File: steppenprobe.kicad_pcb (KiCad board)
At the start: 2 copper layers, 50 x 60 mm, 75 parts, among them J1 USB_C_Receptacle_USB2.0, J2 Conn_01x12, U1 SRV05-4, U2 XC6206PxxxMR, U3 FT2232HL, U4 74LVC1G125, U5 74LVC1G125, U6 74LVC1G125, U7 74LVC1G125, U8 74LVC1G125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

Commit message: Reworked oscillator placement. Fixed silkscreen, added arrows.
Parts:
- moved C5 3.09 mm to (132.0, 67.2), turned to -90 degrees
- moved Y1 2.83 mm to (134.8, 67.0)
- moved C3 1.25 mm to (137.5, 67.2), turned to 90 degrees
- moved FB3 1.13 mm to (132.8, 63.7), turned to 0 degrees
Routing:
- net GND: track 97.0 -> 85.1 mm, vias 39 -> 38
- net /OSCO: track 11.1 -> 8.11 mm
- net /OSCI: track 12.3 -> 13.6 mm
- net /VPHY: track 7.34 -> 8.02 mm

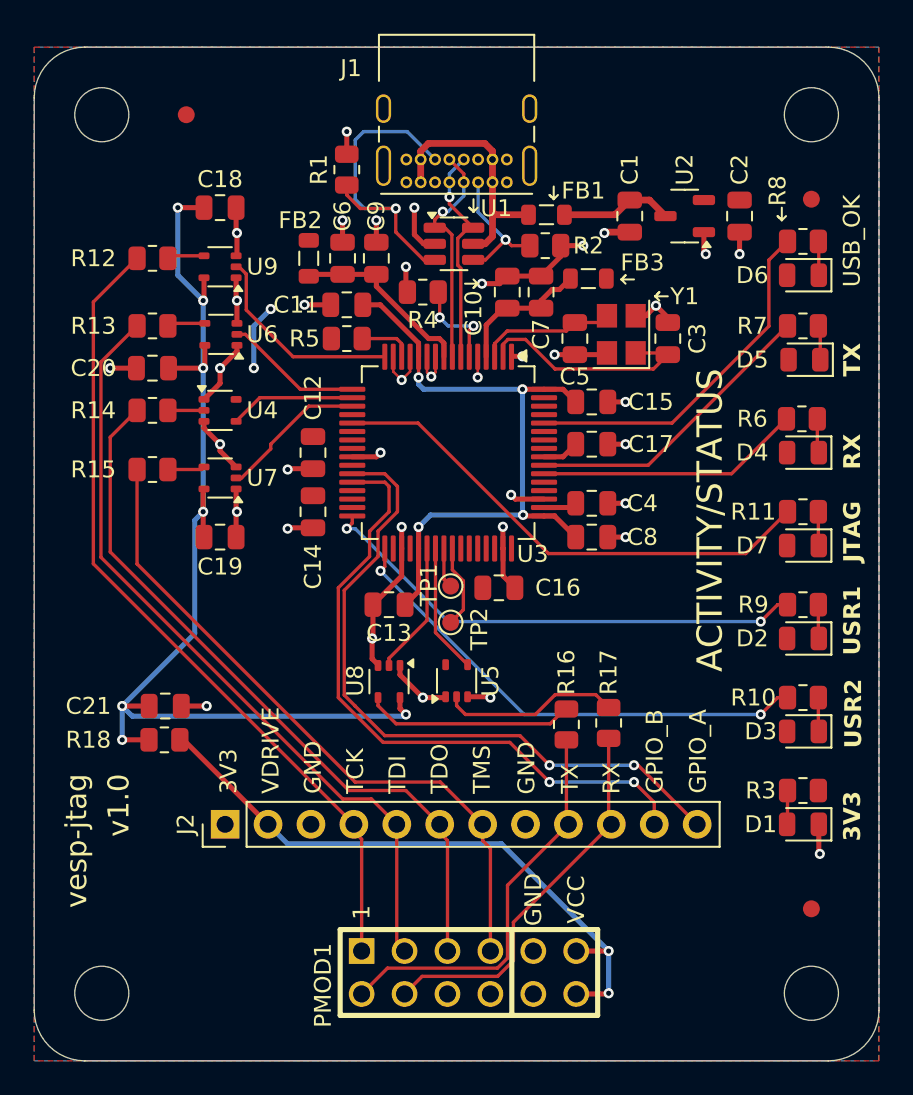
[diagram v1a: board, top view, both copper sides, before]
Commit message: Moved vias closer to pads.
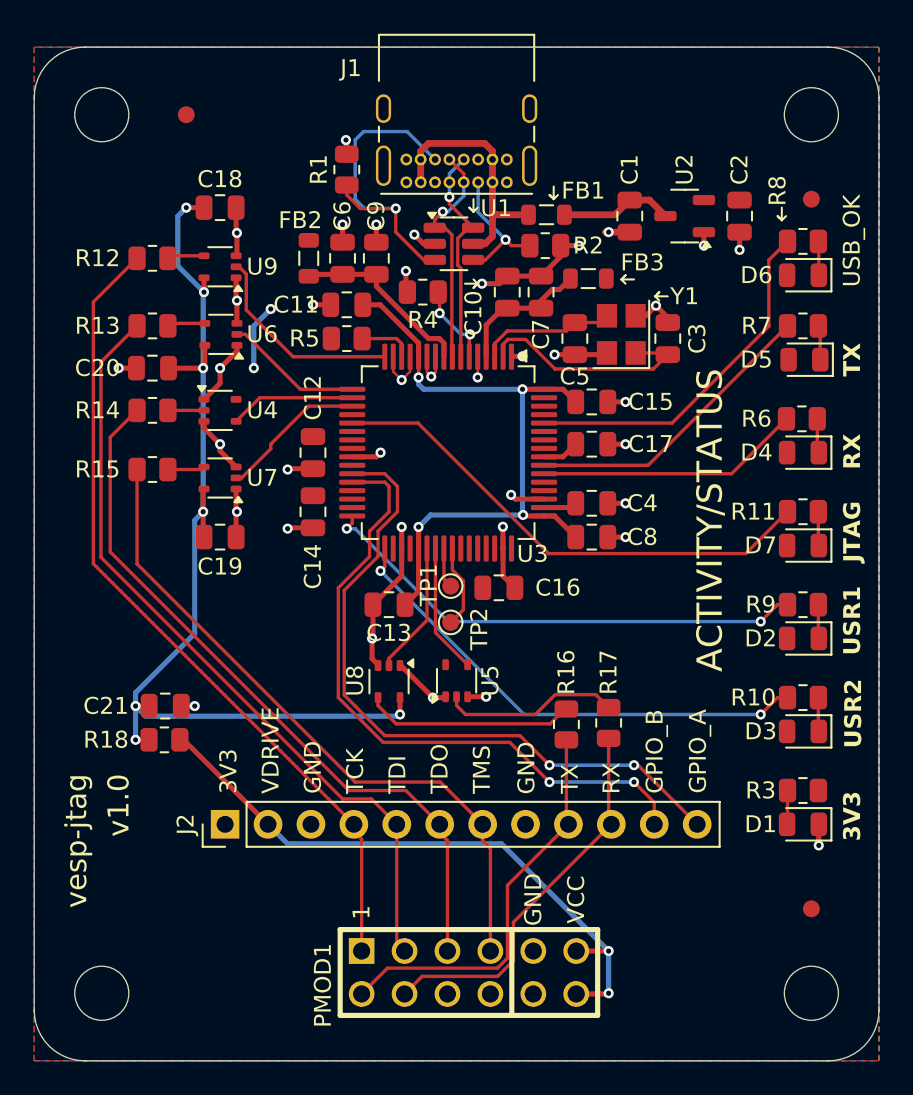
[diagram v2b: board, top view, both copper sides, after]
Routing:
- net GND: track 85.1 -> 78.5 mm
- net Vdrive: track 64.8 -> 60.9 mm
- net /REF: track 5.67 -> 4.95 mm

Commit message: Moved vias, silkscreen alignment.
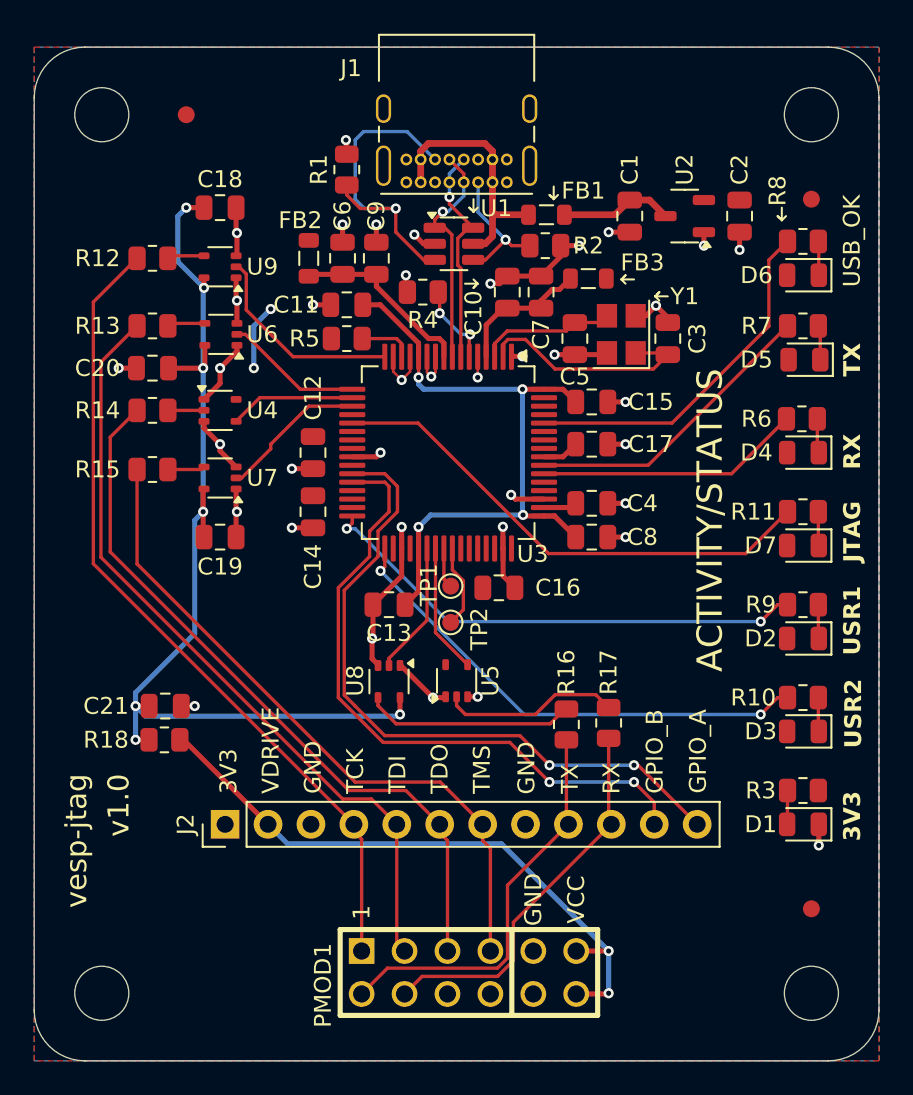
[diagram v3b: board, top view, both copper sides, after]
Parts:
- moved G*** 0.25 mm to (124.8, 63.0)
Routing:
- net GND: track 78.5 -> 76.3 mm

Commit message: Changed export settings.
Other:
- rule pad_to_mask_clearance: 0.05 -> 0
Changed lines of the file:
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@@
 			(dielectric_constraints no)
 		)
-		(pad_to_mask_clearance 0.05)
-		(solder_mask_min_width 0.1)
+		(pad_to_mask_clearance 0)
 		(allow_soldermask_bridges_in_footprints no)
 		(pcbplotparams
-			(layerselection 0x00310fc_ffffffff)
+			(layerselection 0x00010f0_ffffffff)
 			(plot_on_all_layers_selection 0x0000000_00000000)
 			(disableapertmacros no)
 			(usegerberextensions no)
-			(usegerberattributes no)
+			(usegerberattributes yes)
 			(usegerberadvancedattributes no)
-			(creategerberjobfile no)
+			(creategerberjobfile yes)
 			(dashed_line_dash_ratio 12.000000)
 			(dashed_line_gap_ratio 3.000000)
